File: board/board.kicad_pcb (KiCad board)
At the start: 4 copper layers, 61 x 126 mm, 40 parts, among them J1 020_1000BASE-T_with_CT, J10 018_QSPI, J11 Conn_01x03_Male, J2 003_power, J3 008_USB, J4 001_I2C, J5 008_USB, J6 002_SPI, J7 010_UART, J8 015_RGMII, J9 010_UART, U1 VAR-SOM, U2 TLV71318PQDBVRQ1

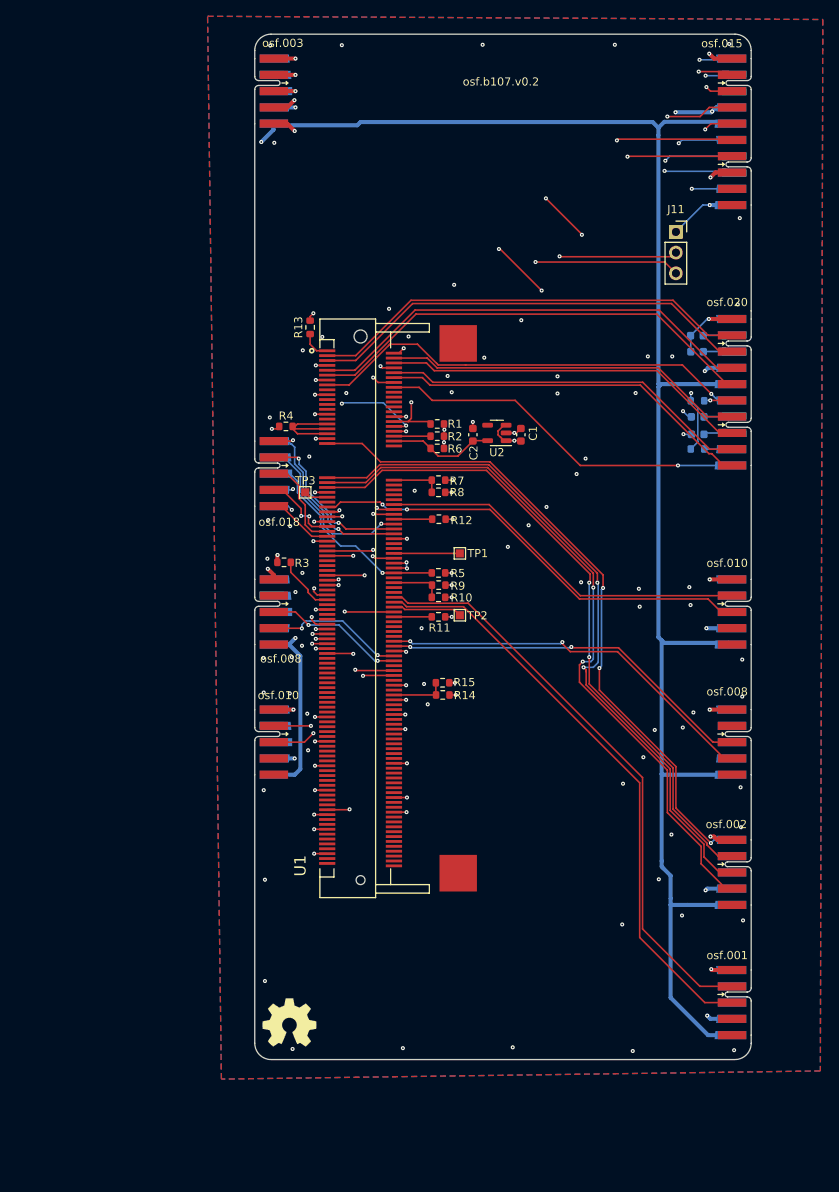
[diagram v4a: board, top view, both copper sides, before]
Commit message: Update PU/PDn and values
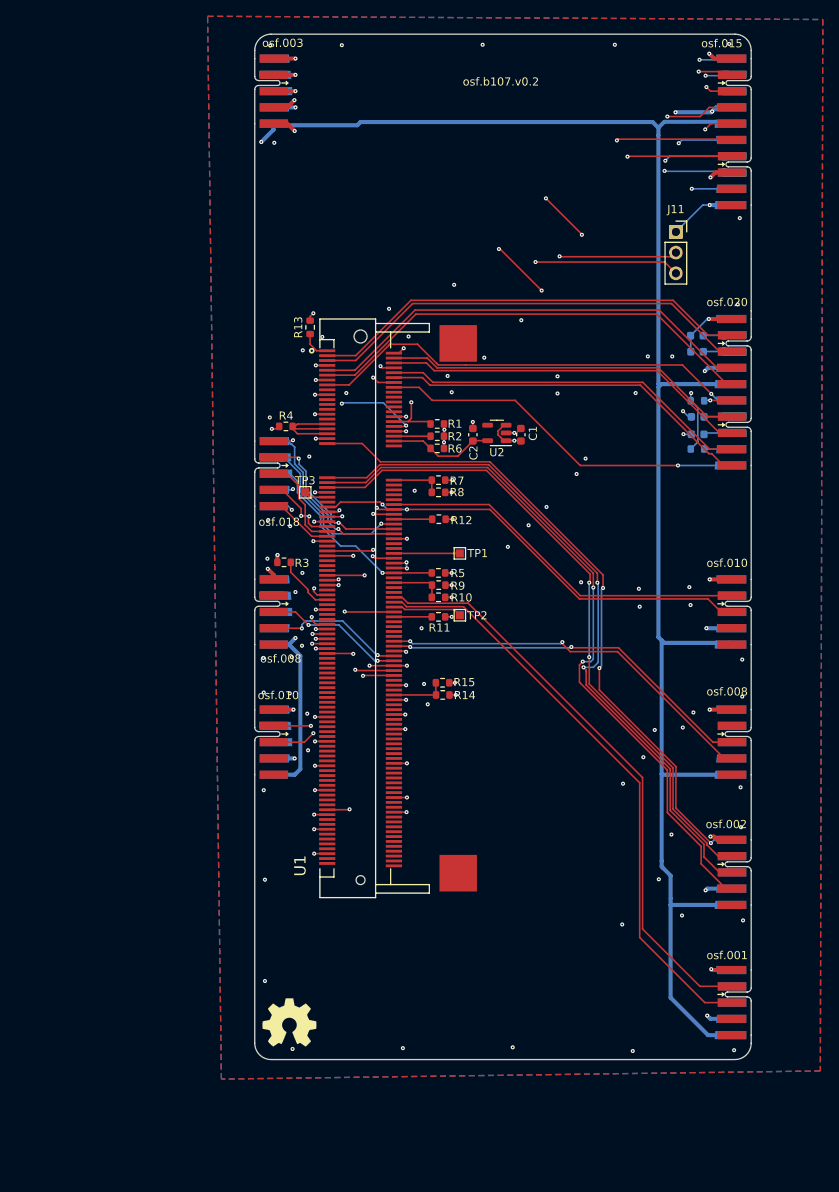
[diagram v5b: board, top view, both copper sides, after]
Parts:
- R1, R14, R9: value 0R -> DNP
- R10: value 560R -> DNP/10k
- R11, R15, R3, R8: value 560R -> 10k
- R12: value 0R -> 0
- R5: value 10k -> DNP/10k
- R7: value 560R -> DNP
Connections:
- U1 pad 118: unconnected-(U1-Pad118) -> GND
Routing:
- net GND: track 121.9 -> 126.5 mm, vias 132 -> 134
